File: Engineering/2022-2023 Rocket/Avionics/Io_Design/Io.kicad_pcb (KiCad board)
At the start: 2 copper layers, 71 parts, among them IC1 AP63300WU-7, IC2 BMP390, J1 PH1-04-UA, J2 TB002-500-08BE, J3 PH1-04-UA, J4 TB002-500-02BE, J5 TB002-500-02BE, J6 MEM2075-00-140-01-A, J7 KMMX-BSMT35S-B30TR, J8 0732511151, Q1 DMG2301L, Q2 CSD17578Q5A, Q3 CSD17578Q5A, Q4 CSD17578Q5A, Q5 CSD17578Q5A, SW1 LSSM12-40-P-V-T/R, U1 LD39150DT33, U2 STM32L486RGT7, U3 USBLC6-2SC6, U4 LSM6DSO32TR, U5 RFM95W-915S2, U6 SAM-M8Q-0-10, Y1 ECS-400-10-37B2-CKM-TR

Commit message: First PCB draft done. p a i n
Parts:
- removed R18: 1.5k, Resistor_SMD:R_0402_1005Metric
- moved R5 107.0 mm to (144.0, 130.7), turned to 0 degrees
- moved Q5 102.5 mm to (145.3, 135.0), turned to -90 degrees
- moved R4 100.2 mm to (136.8, 130.7), turned to 0 degrees
- moved Q4 96.4 mm to (138.1, 135.0), turned to -90 degrees
- moved J3 82.8 mm to (165.8, 70.7)
- moved R12 81.6 mm to (141.8, 139.7), turned to 180 degrees
- moved R3 81.0 mm to (129.2, 128.6), turned to 0 degrees
- moved Q3 79.1 mm to (131.0, 135.0), turned to -90 degrees
- moved R10 78.1 mm to (136.3, 139.7), turned to 180 degrees
- moved R2 77.4 mm to (122.5, 130.7), turned to 0 degrees
- moved R13 76.7 mm to (140.7, 130.5), turned to 180 degrees
- moved J7 76.4 mm to (164.0, 88.9), turned to 90 degrees
- moved R8 76.2 mm to (131.3, 139.7), turned to 180 degrees
- moved R6 75.6 mm to (127.2, 138.6)
- moved Q2 75.5 mm to (123.8, 135.0), turned to -90 degrees
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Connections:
- J6 pad P1: (no net) -> SDMMC_D2
- J6 pad P2: (no net) -> SDMMC_D3
- J6 pad P3: (no net) -> SDMMC_CMD
- J6 pad P4: (no net) -> +3.3V
- J6 pad P5: (no net) -> SDMMC_CLK
- J6 pad P6: (no net) -> GND
- J6 pad P7: (no net) -> SDMMC_D0
- J6 pad P8: (no net) -> SDMMC_D1
- J6 pad P9: (no net) -> SDMMC_DET
- J6 pad SH1: (no net) -> GND
- J6 pad SH2: (no net) -> GND
- J6 pad SH3: (no net) -> GND
- J6 pad SH4: (no net) -> GND
- U3 pad 1: /USB_D+ -> /USB_D-
- U3 pad 3: /USB_D- -> /USB_D+
- U3 pad 4: USB_ESD_D- -> USB_ESD_D+
- U3 pad 6: USB_ESD_D+ -> USB_ESD_D-
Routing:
- net +3.3V: track 0.00 -> 231.6 mm, vias 0 -> 19
- net GND: track 22.9 -> 160.8 mm, vias 2 -> 52
- net ARM: track 4.53 -> 141.8 mm, vias 0 -> 2
- net VBUS: track 0.00 -> 55.2 mm, vias 0 -> 2
- net PYRO4_DET: track 2.67 -> 51.9 mm, vias 0 -> 2
- net PYRO3_DET: track 2.57 -> 47.1 mm, vias 0 -> 2
- net PYRO2_DET: track 2.60 -> 44.1 mm, vias 0 -> 2
- net PYRO1_DET: track 2.36 -> 41.7 mm, vias 0 -> 2
- net SWCLK: track 0.00 -> 39.1 mm, vias 0 -> 4
- net SWDIO: track 0.00 -> 35.9 mm, vias 0 -> 2
- net PYRO1: track 2.85 -> 37.9 mm
- net SDMMC_DET: track 0.00 -> 34.9 mm
- net SDMMC_D0: track 0.00 -> 33.4 mm, vias 0 -> 2
- net SDMMC_D1: track 0.00 -> 32.8 mm
- net PYRO4: track 0.00 -> 31.0 mm
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- added copper zone on B.Cu, net GND

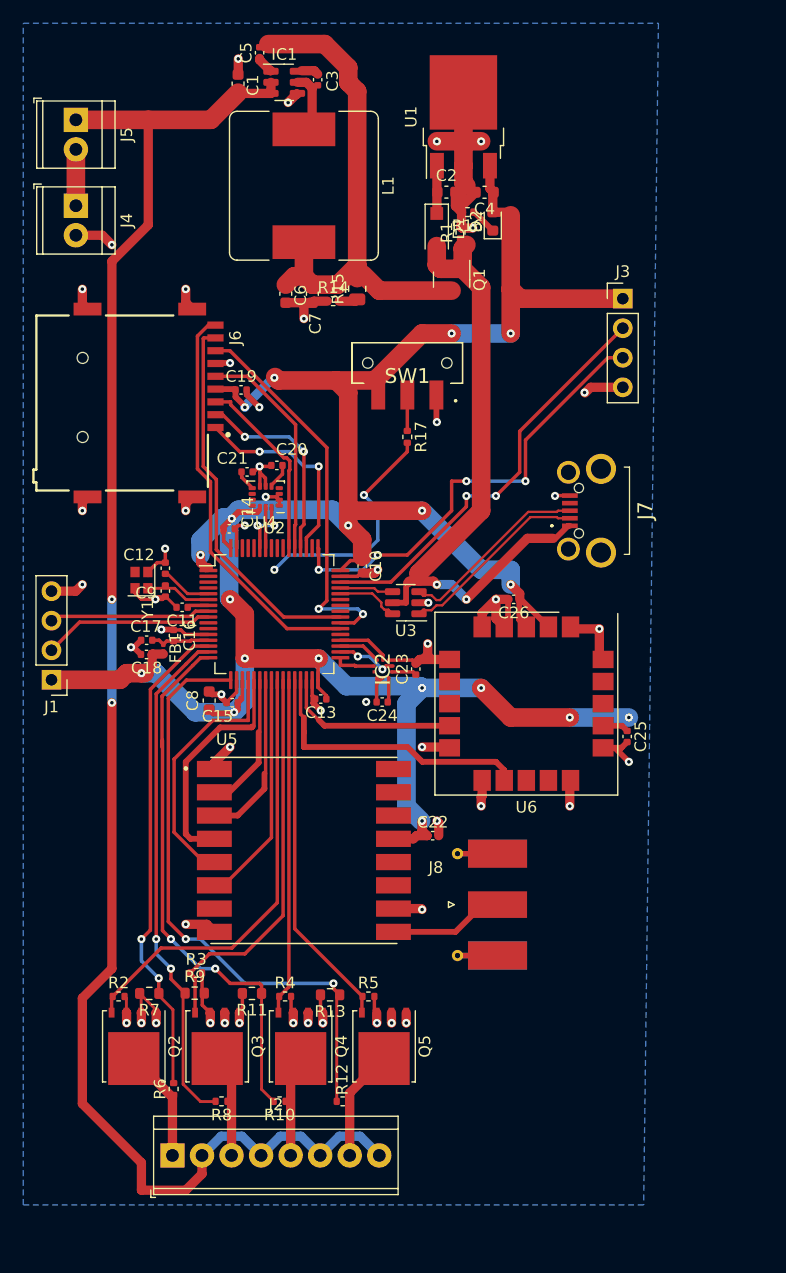
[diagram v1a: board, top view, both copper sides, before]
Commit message: Redesigned with 4-layer board
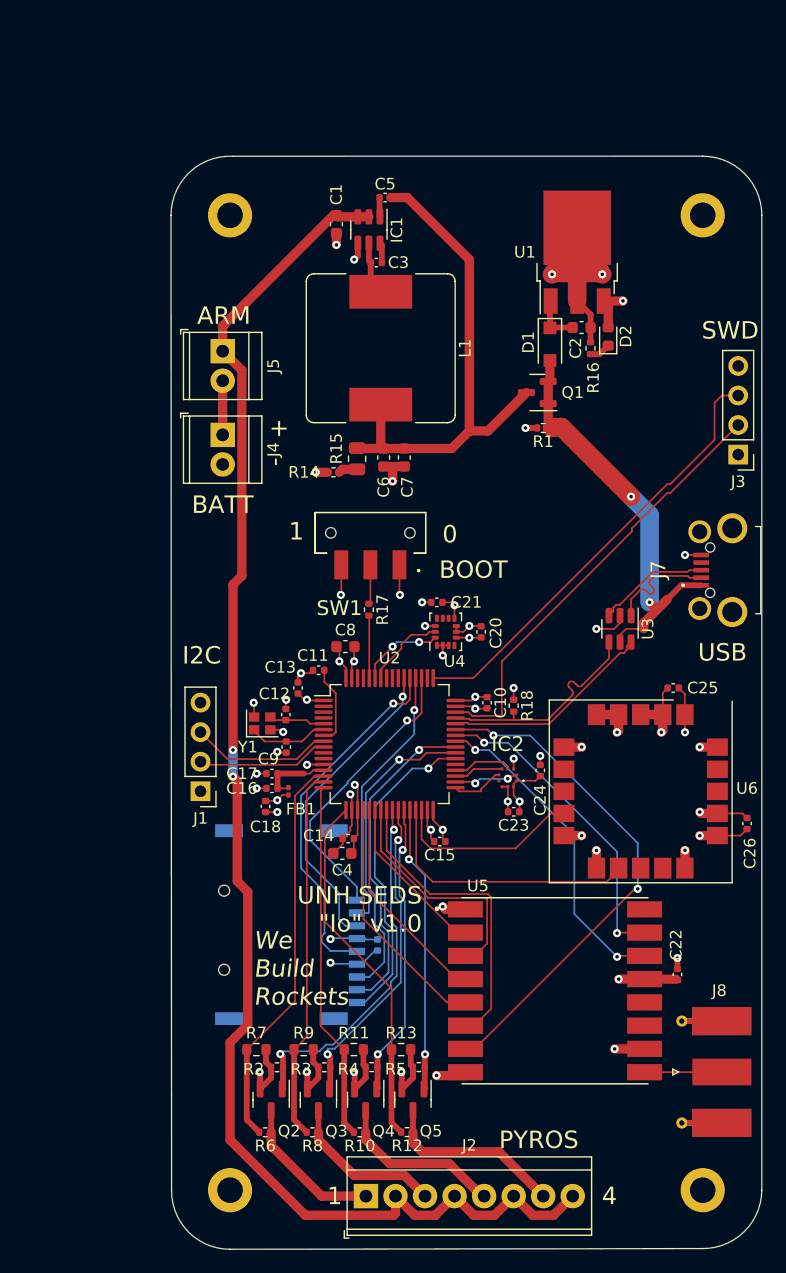
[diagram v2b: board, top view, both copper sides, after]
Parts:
- added H1: MountingHole_2.2mm_M2_DIN965_Pad, MountingHole:MountingHole_2.2mm_M2_DIN965_Pad, F.Cu at (132.1, 63.5)
- added H2: MountingHole_2.2mm_M2_DIN965_Pad, MountingHole:MountingHole_2.2mm_M2_DIN965_Pad, F.Cu at (172.7, 63.5)
- added H3: MountingHole_2.2mm_M2_DIN965_Pad, MountingHole:MountingHole_2.2mm_M2_DIN965_Pad, F.Cu at (172.7, 147.3)
- added H4: MountingHole_2.2mm_M2_DIN965_Pad, MountingHole:MountingHole_2.2mm_M2_DIN965_Pad, F.Cu at (132.1, 147.3)
- added R18: 1.5k, Resistor_SMD:R_0402_1005Metric, F.Cu at (156.5, 105.7)
- C19, J6: moved to B.Cu
- Q2, Q3, Q4, Q5: value CSD17578Q5A -> DMG2302U; footprint Package_TO_SOT_SMD:TDSON-8-1 -> Package_TO_SOT_SMD:SOT-23
- moved C4 58.1 mm to (141.7, 118.4)
- moved C19 49.1 mm to (144.8, 126.2), turned to -90 degrees
- moved J6 47.4 mm to (131.6, 125.0), turned to 90 degrees
- moved C14 28.5 mm to (142.2, 117.1), turned to 180 degrees
- moved C26 27.8 mm to (176.5, 115.8), turned to -90 degrees
- moved U5 24.7 mm to (160.0, 130.2)
- moved C22 24.2 mm to (170.5, 128.8), turned to 90 degrees
- moved J8 24.1 mm to (172.6, 137.2)
- moved J5 23.6 mm to (131.4, 75.2)
- moved J4 23.4 mm to (131.4, 82.4)
- moved C20 22.7 mm to (153.7, 99.3), turned to 90 degrees
- moved C15 21.5 mm to (150.1, 117.3)
- moved C21 19.8 mm to (149.9, 96.8), turned to 180 degrees
- moved U4 19.3 mm to (150.6, 99.3), turned to 90 degrees
- moved U3 18.6 mm to (165.6, 99.1), turned to -90 degrees
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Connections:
- net Net-(C16-Pad1) renamed VDDA
- net Net-(C2-Pad1) renamed /LDO_D
- net Net-(C3-Pad1) renamed /5V_I
- net Net-(C3-Pad2) renamed /5V_C
- net Net-(D2-Pad1) renamed /LDO_LED
- net Net-(J8-Pad1) renamed /RF_ANT
- net Net-(R14-Pad2) renamed /5V_R
- J6 pad SH1: GND -> (no net)
- J6 pad SH2: GND -> (no net)
- J6 pad SH3: GND -> (no net)
- J6 pad SH4: GND -> (no net)
- Q2 pad 1: GND -> PYRO1
- Q2 pad 3: GND -> PYRO1_SW
- Q3 pad 1: GND -> PYRO2
- Q3 pad 3: GND -> PYRO2_SW
- Q4 pad 1: GND -> PYRO3
- Q4 pad 3: GND -> PYRO3_SW
- Q5 pad 1: GND -> PYRO4
- Q5 pad 3: GND -> PYRO4_SW
- U2 pad 41: unconnected-(U2-Pad41) -> RF_DIO0
- U2 pad 42: unconnected-(U2-Pad42) -> RF_DIO1
- U2 pad 43: unconnected-(U2-Pad43) -> RF_DIO5
- U5 pad 14: unconnected-(U5-Pad14) -> RF_DIO0
- U5 pad 15: unconnected-(U5-Pad15) -> RF_DIO1
- U5 pad 7: unconnected-(U5-Pad7) -> RF_DIO5
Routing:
- net +3.3V: track 231.6 -> 56.5 mm, vias 19 -> 17
- net RF_DIO5: track 0.00 -> 44.2 mm, vias 0 -> 2
- net GND: track 160.8 -> 117.0 mm, vias 52 -> 46
- net RF_DIO0: track 0.00 -> 27.9 mm, vias 0 -> 2
- net RF_DIO1: track 0.00 -> 27.4 mm, vias 0 -> 2
- net PYRO4_DET: track 51.9 -> 31.2 mm, vias 2 -> 0
- net VBUS: track 55.2 -> 35.6 mm
- net PYRO3_DET: track 47.1 -> 30.9 mm, vias 2 -> 0
- net ARM: track 141.8 -> 126.5 mm
- net /BOOT0: track 20.4 -> 5.34 mm, vias 2 -> 0
- net USB_ESD_D+: track 4.62 -> 18.8 mm
- net USB_ESD_D-: track 5.42 -> 18.2 mm
- net PYRO2_DET: track 44.1 -> 32.1 mm, vias 2 -> 0
- net SDMMC_CLK: track 19.3 -> 31.0 mm, vias 0 -> 1
- net SDMMC_CMD: track 16.2 -> 27.2 mm, vias 0 -> 1
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- added copper zone on In2.Cu, net +3.3V
- added copper zone on In1.Cu, net GND
- removed copper zone on B.Cu, net GND
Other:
- board outline added: 50.8 x 94 mm
- copper layers 2 -> 4
- board text added: "+"
- board text added: "-"
- board text added: "0"
- board text added: "1"
- board text added: "4"
- board text added: "ARM"
- board text added: "BATT"
- board text added: "BOOT"
- board text added: "I2C"
- board text added: "PYROS"
- board text added: "SWD"
- board text added: "UNH SEDS {dblquote}Io{dblquote} v1.0"
- board text added: "USB"
- board text added: "We Build Rockets"

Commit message: Finalized PCB design
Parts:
- H1, H2, H3, H4: value MountingHole_2.2mm_M2_DIN965_Pad -> MountingHole_3.2mm_M3_Pad; footprint MountingHole:MountingHole_2.2mm_M2_DIN965_Pad -> MountingHole:MountingHole_3.2mm_M3_Pad
- moved H2 1.80 mm to (171.4, 64.8)
- moved H1 1.80 mm to (133.3, 64.8)
- moved R10 1.12 mm to (143.2, 141.2)
- moved R6 1.12 mm to (135.1, 141.2)
- moved R8 1.12 mm to (139.2, 141.2)
- moved R12 1.10 mm to (147.3, 141.2)
- moved H4 1.08 mm to (132.8, 146.6)
- moved R2 0.86 mm to (136.1, 135.9)
- moved R3 0.86 mm to (140.2, 135.9)
- moved J2 0.86 mm to (143.8, 147.0)
- moved Q2 0.86 mm to (135.6, 138.7)
- moved Q3 0.86 mm to (139.7, 138.7)
- moved Q4 0.86 mm to (143.7, 138.7)
- moved Q5 0.86 mm to (147.8, 138.7)
- moved R11 0.86 mm to (142.7, 134.4)
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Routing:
- net PYRO2_DET: track 32.1 -> 34.2 mm
- net PYRO1_DET: track 34.3 -> 33.3 mm
- net PYRO4_DET: track 31.2 -> 30.2 mm
- net PYRO4: track 24.6 -> 23.8 mm
- net PYRO2: track 27.6 -> 28.3 mm
